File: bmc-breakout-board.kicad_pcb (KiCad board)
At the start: 2 copper layers, 90 x 60 mm, 20 parts, among them J1 PinHeader_2x4, J10 PinHeader_2x4, J11 PinHeader_2x05, J12 61300411121, J13 0473460001, J14 PCIE_BUS_x1, J15 0473460001, J16 PinHeader_1x07, J2 PinHeader_2x13, J3 PinHeader_2x08, J4 61300411121, J5 ME1016813401101, J6 61300411121, J7 DC_SOCKET, J8 PinHeader_2x05, J9 PinHeader_1x07

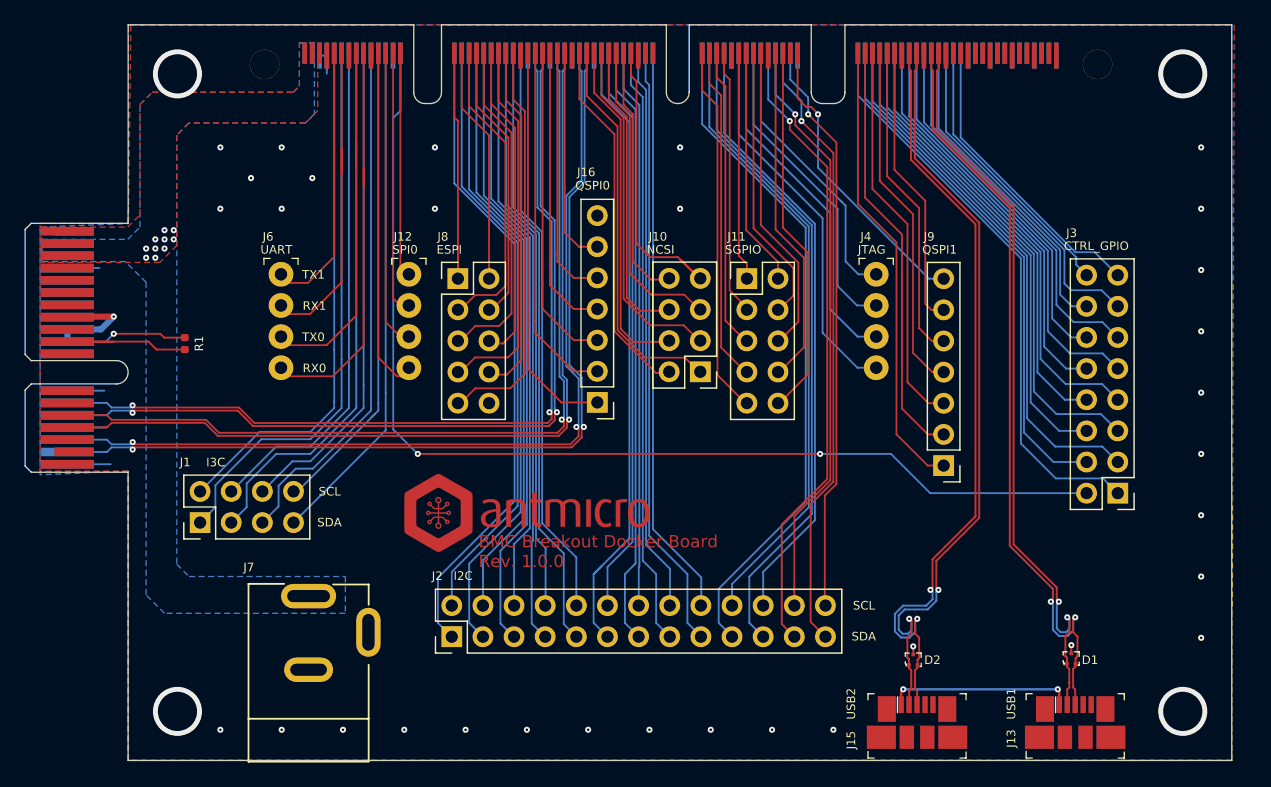
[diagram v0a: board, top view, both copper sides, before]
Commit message: Add 2 inner layers, stackup and reroute PCIe
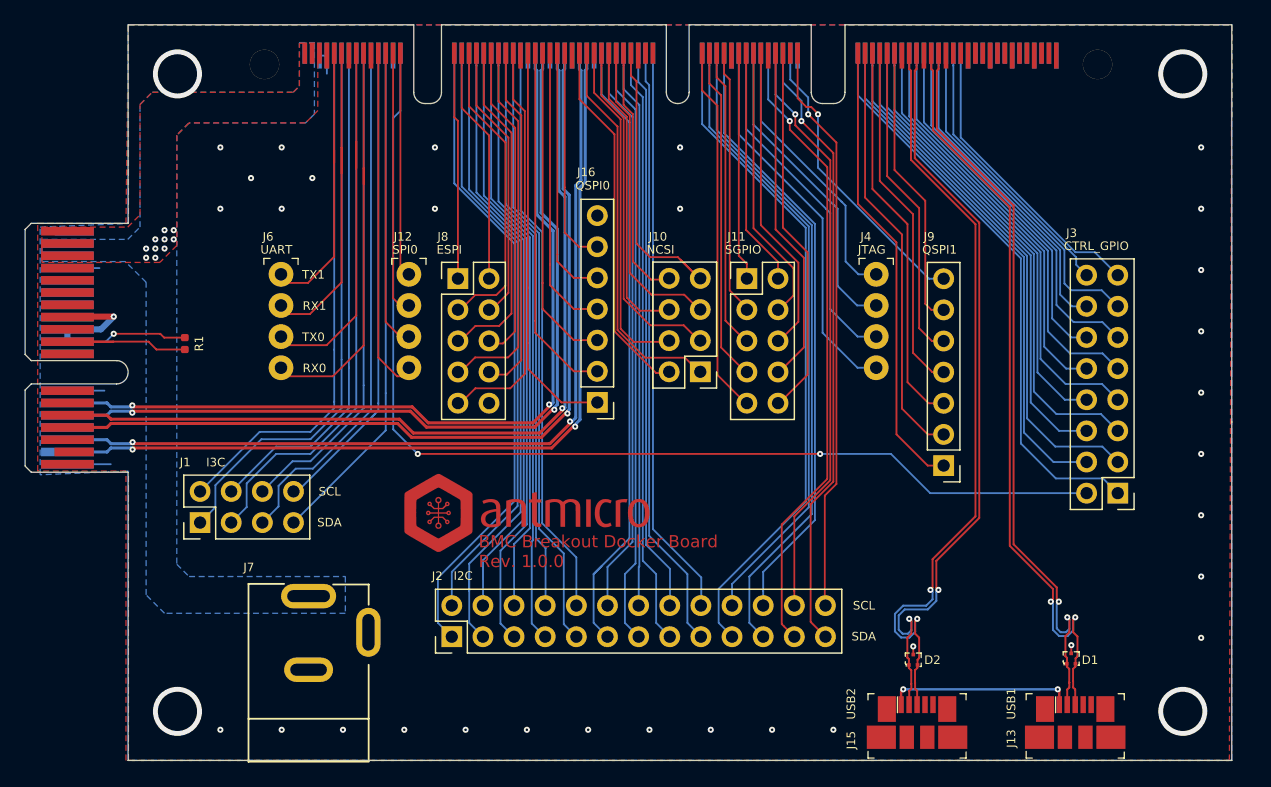
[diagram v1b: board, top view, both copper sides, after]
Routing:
- net PCIE_BMC_RX_P: track 74.6 -> 72.7 mm
- net PCIE_BMC_RX_N: track 75.1 -> 73.2 mm
- net PCIE_BMC_TX_P: track 72.1 -> 71.3 mm
- net PCIE_BMC_CLK_100_P: track 71.0 -> 70.3 mm
- net PCIE_BMC_TX_N: track 72.5 -> 71.9 mm
- net PCIE_BMC_CLK_100_N: track 71.4 -> 70.9 mm
- added copper zone on In1.Cu, net GND
- added copper zone on In2.Cu, net P12V_AUX
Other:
- copper layers 2 -> 4
- net class PCIe: trace_width 0.11 -> 0.25
- board text added: "0.018 mm"
- board text added: "0.02 mm"
- board text added: "0.035 mm"
- board text added: "0.36 mm"
- board text added: "0.71 mm"
- board text added: "1"
- board text added: "2"
- board text added: "3"
- board text added: "3.5"
- board text added: "4"
- board text added: "4.2"
- board text added: "4.6"
- board text added: "5"
- board text added: "6"
- board text added: "7"
- board text added: "8"
- board text added: "9"
- board text added: "Bottom Layer"
- board text added: "Bottom Solder"
- board text added: "Constant"
- board text added: "Copper"
- board text added: "Dielectric 1"
- board text added: "Dielectric 2"
- board text added: "Dielectric 3"
- board text added: "FR-4"
- board text added: "Gold plating (ENIG, selective)"
- board text added: "Layer"
- board text added: "Material"
- board text added: "Name"
- board text added: "Prepreg"
- board text added: "Recommended PCB finish:"
- board text added: "Recommended PCB stackup"
- board text added: "Signal 1"
- board text added: "Signal 2"
- board text added: "Silkscreen: white"
- board text added: "Solder Resist"
- board text added: "Solder mask: matt black"
- board text added: "Suggested prepreg material is ISOLA PR2116"
- board text added: "The design includes high speed signaling"
- board text added: "Thickness"
- board text added: "Top Layer"
- board text added: "Top Solder"
- board text removed: "1. Copper F.Cu 0.035 -- 2116 0.12 4.5 2. Copper GND1 0.035 -- FR4 0.23 4.6 3. Copper In2 0.035 -- 7630 0.2 4.7 4. Copper VCC1 0.035 -- FR4 0.23 4.6 5. Copper GND2 0.035 -- 7630 0.2 4.5 6. Copper In5 0.035 -- FR4 0.23 4.6 7. Copper VCC2 0.035 -- 2116 0.12 4.6 8. Copper B.Cu 0.035"

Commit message: Change size of the vias
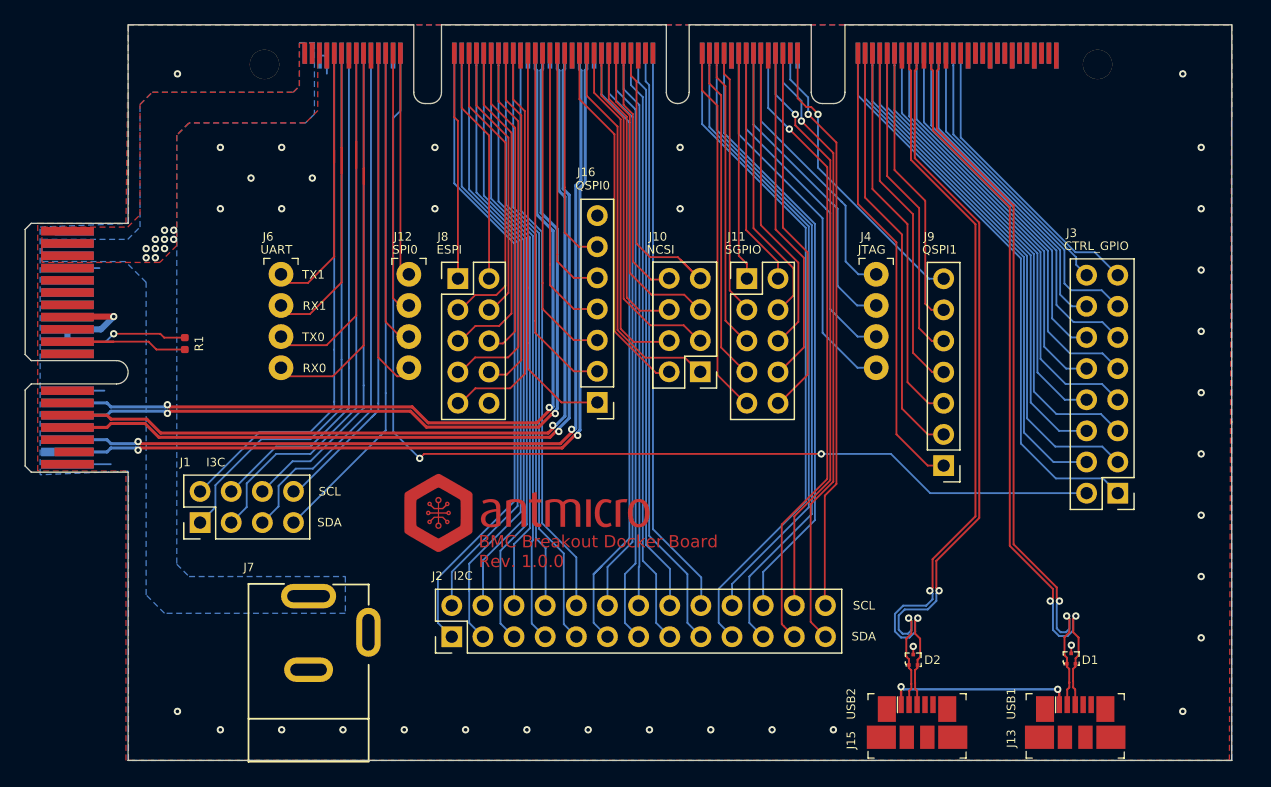
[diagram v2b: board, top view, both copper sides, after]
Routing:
- net PCIE_BMC_RX_P: track 72.7 -> 73.2 mm
- net PCIE_BMC_RX_N: track 73.2 -> 73.8 mm

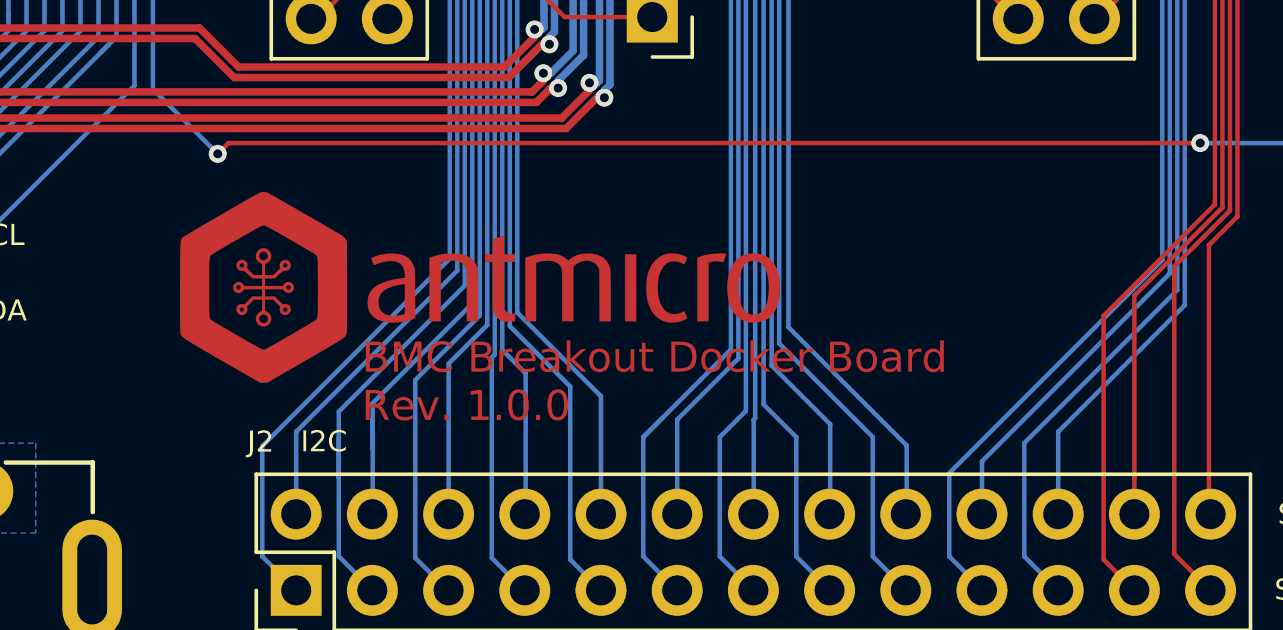
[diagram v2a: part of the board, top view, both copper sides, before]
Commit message: Edit logo
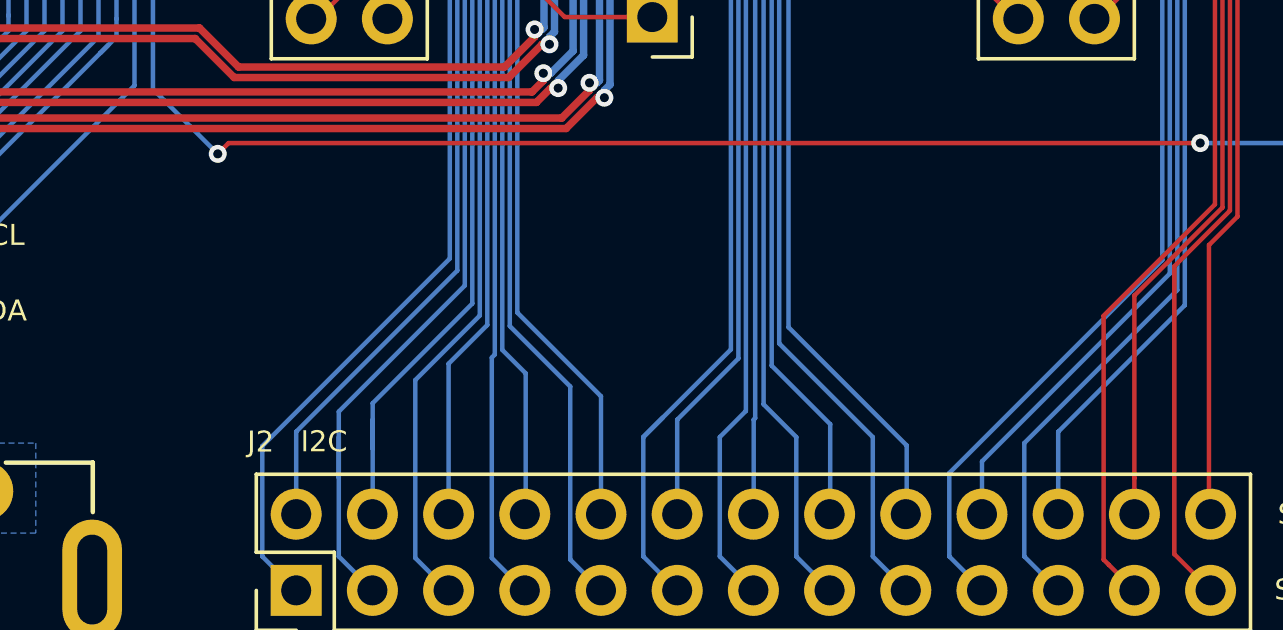
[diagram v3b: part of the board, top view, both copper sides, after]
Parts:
- D1, D2: footprint antmicro-footprints:SOT-3 -> bmc-breakout-board-footprints:SOT-3
- J1, J10: footprint antmicro-footprints:PinHeader_2x04_P2.54mm_Vertical -> bmc-breakout-board-footprints:PinHeader_2x04_P2.54mm_Vertical
- J11, J8: footprint antmicro-footprints:PinHeader_2x05_P2.54mm_Vertical -> bmc-breakout-board-footprints:PinHeader_2x05_P2.54mm_Vertical
- J12, J4, J6: footprint antmicro-footprints:PinHeader_1x4_P2.54mm_Drill1.02mm -> bmc-breakout-board-footprints:PinHeader_1x4_P2.54mm_Drill1.02mm
- J13, J15: footprint antmicro-footprints:USB_Micro_B_Female_0473460001 -> bmc-breakout-board-footprints:USB_Micro_B_Female_0473460001
- J14: footprint antmicro-footprints:BUS_PCIexpress_x1 -> bmc-breakout-board-footprints:BUS_PCIexpress_x1
- J16, J9: footprint antmicro-footprints:PinHeader_1x07_P2.54mm_Vertical -> bmc-breakout-board-footprints:PinHeader_1x07_P2.54mm_Vertical
- J2: footprint antmicro-footprints:PinHeader_2x13_P2.54mm_Vertical -> bmc-breakout-board-footprints:PinHeader_2x13_P2.54mm_Vertical
- J3: footprint antmicro-footprints:PinHeader_2x08_P2.54mm_Vertical -> bmc-breakout-board-footprints:PinHeader_2x08_P2.54mm_Vertical
- J5: footprint antmicro-footprints:ME1016813401101 -> bmc-breakout-board-footprints:ME1016813401101
- J7: footprint antmicro-footprints:DC_SOCKET -> bmc-breakout-board-footprints:DC_SOCKET
- N1: footprint antmicro-footprints:antmicro-logo_scaled_20mm -> bmc-breakout-board-footprints:antmicro-logo_scaled_20mm_mask
- R1: footprint antmicro-footprints:0402-res -> bmc-breakout-board-footprints:0402-res

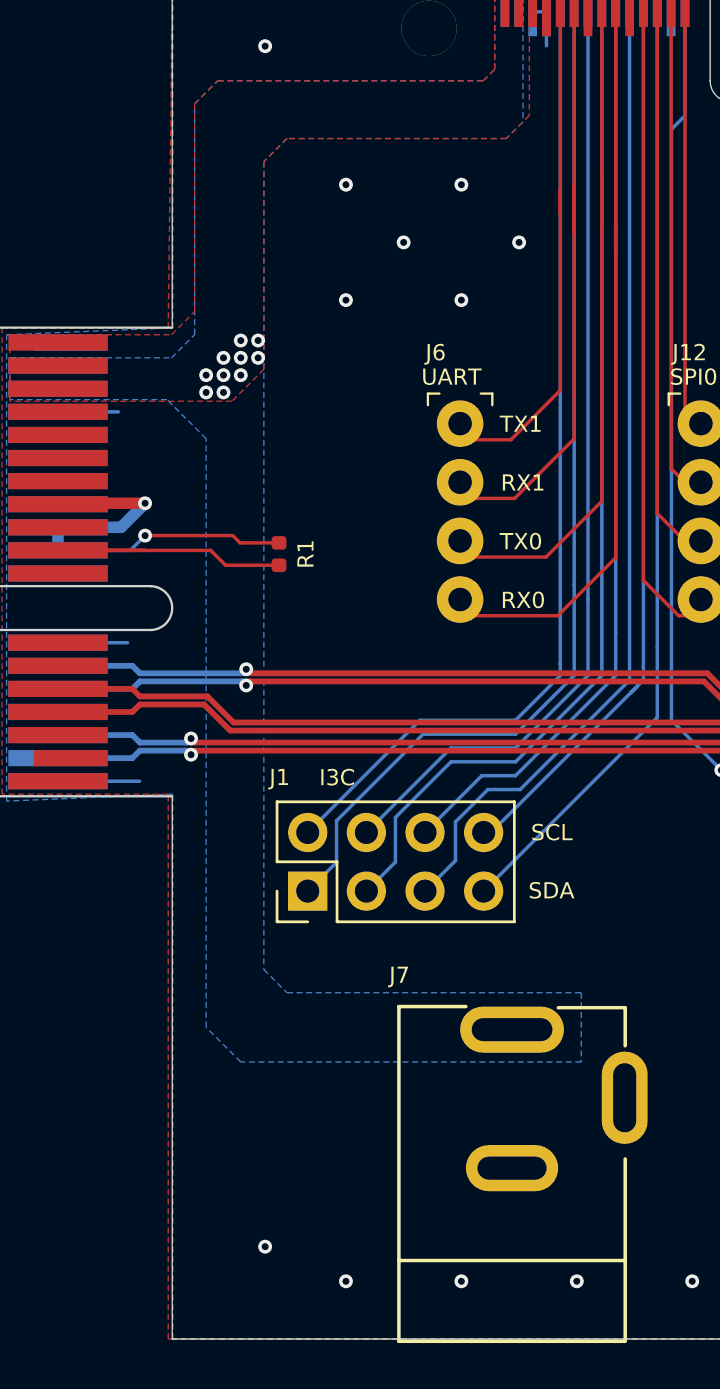
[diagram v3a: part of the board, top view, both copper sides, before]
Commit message: Add a power switch
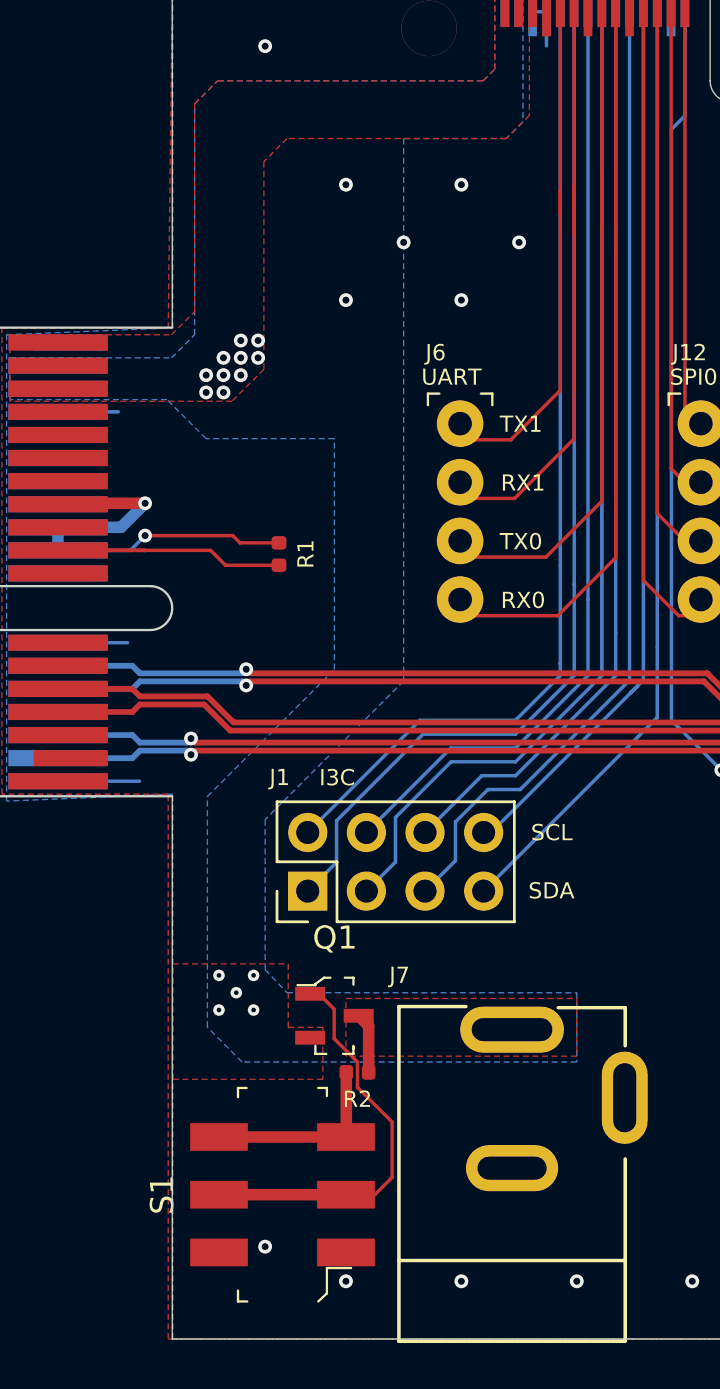
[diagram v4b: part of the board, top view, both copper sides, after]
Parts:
- added Q1: BSS138AKA, bmc-breakout-board-footprints:SOT-23-3, F.Cu at (67.1, 108.7)
- added R2: R_10k_0402, bmc-breakout-board-footprints:0402-res, F.Cu at (68.1, 111.1)
- added S1: JS202011SCQN, bmc-breakout-board-footprints:Switch_Slide_JS202011SCQN, F.Cu at (64.8, 116.4)
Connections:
- J7 pad 1: P12V_AUX -> P12V_IN
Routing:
- net Net-(Q1-Pad1): track 0.00 -> 17.5 mm
- net Net-(R2-Pad2): track 0.00 -> 8.31 mm
- net P12V_IN: track 0.00 -> 2.77 mm
- net P12V_AUX: vias 10 -> 15
- added copper zone on F.Cu, net P12V_IN
